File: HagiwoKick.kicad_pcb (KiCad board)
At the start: 2 copper layers, 30 x 106 mm, 37 parts, among them J1 Tune In, J2 Eurorack_Power_16pin_Shrouded, J3 A. Out, J4 Trig In

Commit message: latest updates
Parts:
- removed Attack, Decay, Harmonic, Tone: 100K, Library:Pot_9mm_DShaft_RemovedPins4_5
- removed J4: Trig In, Library:EighthInch_PJ398SM_T_TN_S
- added PWR1: Eurorack_Power_10pin_Unshrouded, Library:IDC-Header_2x05_P2.54mm_Vertical_Euro_Power_Striped_ThickerText, B.Cu at (56.9, 111.7)
- added RV1: 100k, Library:Pot_9mm_DShaft_RemovedPins4_5, F.Cu at (66.0, 57.1)
- added RV2: 100k, Library:Pot_9mm_DShaft_RemovedPins4_5, F.Cu at (66.0, 76.8)
- added RV3: 100k, Library:Pot_9mm_DShaft_RemovedPins4_5, F.Cu at (66.0, 116.1)
- added RV4: 100k, Library:Pot_9mm_DShaft_RemovedPins4_5, F.Cu at (66.0, 96.5)
- C1, C2, C3, C4, C5: value 101 -> 100pF
- C10: value 222 -> 2.2nF
- C6: value 104 -> 100nF
- C7: footprint Capacitor_THT:CP_Radial_D5.0mm_P2.50mm -> Capacitor_THT:CP_Radial_D4.0mm_P1.50mm
- C8: value 225 -> 2.2uF
- C9: value 474 -> 470nF
- D1, D2, D3, D4, D5, D6: value B43 -> BAT43; footprint Diode_THT:D_DO-35_SOD27_P7.62mm_Horizontal -> Library:D_DO-35_SOD27_P7.62mm_Horizontal_Widened_No_K
- J1: value Tune In -> TUNE CV; footprint Library:EighthInch_PJ398SM_T_TN_S -> Library:EighthInch_PJ398SM_3mmNPTH
- J2: value Eurorack_Power_16pin_Shrouded -> OUT; footprint PCM_4ms_Connector:Pins_2x08_2.54mm_TH_EuroPower_Shrouded -> Library:EighthInch_PJ398SM_3mmNPTH; moved to F.Cu
- J3: value A. Out -> TRIG; footprint Library:EighthInch_PJ398SM_T_TN_S -> Library:EighthInch_PJ398SM_3mmNPTH
- R1, R10, R2, R3, R4, R5: value 1K -> 1k
- R6, R8: value 100K -> 100k
- R7: value 33K -> 33k
- moved R1 77.3 mm to (77.5, 64.1), turned to -90 degrees
- moved C1 75.4 mm to (77.5, 74.9), turned to -90 degrees
- moved D3 69.9 mm to (67.6, 136.7), turned to -90 degrees
- moved D4 67.6 mm to (64.5, 136.7), turned to -90 degrees
- moved C8 51.6 mm to (54.6, 64.1)
- moved D1 41.1 mm to (67.6, 147.1), turned to -90 degrees
- moved D2 38.9 mm to (64.5, 147.1), turned to -90 degrees
- moved J2 35.9 mm to (58.4, 148.8), turned to -90 degrees
- moved C9 35.3 mm to (54.6, 80.6)
- moved R4 33.3 mm to (77.5, 116.1)
- moved C2 31.9 mm to (77.5, 88.8)
- moved C6 31.6 mm to (73.7, 101.4), turned to 90 degrees
- moved R2 27.7 mm to (77.5, 99.6)
- moved C7 24.4 mm to (59.4, 103.4), turned to 180 degrees
- moved D5 23.7 mm to (62.2, 109.0), turned to 0 degrees
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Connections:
- C10 pad 2: Net-(C10-Pad2) -> Net-(J2-SIG)
- J2 pad 1: Net-(J2-P1) -> Net-(J2-SIG)
- J2 pad 2: Net-(J2-P1) -> unconnected-(J2-SHEILD-Pad2)
- J2 pad 3: Net-(J2-P3) -> GND
- R10 pad 2: Net-(J4-PadT) -> Net-(J3-SIG)
- R5 pad 1: Net-(J1-PadT) -> Net-(J1-SIG)
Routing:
- net A0: track 131.5 -> 11.2 mm
- net D10: track 27.6 -> 129.1 mm, vias 3 -> 0
- net Net-(J3-SIG): track 0.00 -> 71.8 mm
- net Net-(C8-Pad1): track 80.0 -> 9.47 mm, vias 4 -> 0
- net Net-(J4-PadT): track 53.7 -> 0.00 mm
- net Net-(D7-A): track 138.5 -> 85.9 mm
- net A1: track 66.4 -> 25.8 mm
- net Net-(C10-Pad1): track 104.3 -> 66.9 mm, vias 2 -> 0
- net Net-(R3-Pad1): track 44.0 -> 10.5 mm
- net A5: track 31.6 -> 56.9 mm
- net Net-(R2-Pad1): track 46.4 -> 21.2 mm, vias 4 -> 0
- net Net-(J1-PadT): track 24.9 -> 0.00 mm
- net +5V: track 87.3 -> 110.6 mm
- net +12V: track 54.5 -> 36.2 mm
- net GND: track 13.8 -> 0.00 mm
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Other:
- board text added: "SynthLab"
- board text added: "`TR KICK` BY HAGIWO"
- board text added: "github.com/fablabnk/SynthLabProjects"
- board text removed: "`TR KICK` ORIGINAL DESIGN BY HAGIWO"

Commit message: v1.1 ready for final check
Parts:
- C7: footprint Capacitor_THT:CP_Radial_D4.0mm_P1.50mm -> Capacitor_THT:CP_Radial_D4.0mm_P2.00mm
- RV1, RV2, RV3, RV4: value 100k -> 100k B
- moved C7 0.26 mm to (59.7, 103.4)
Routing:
- net A5: track 56.9 -> 82.7 mm
- net Net-(J3-SIG): track 71.8 -> 46.8 mm
- net D10: track 129.1 -> 117.5 mm, vias 0 -> 2
- net Net-(D7-A): track 85.9 -> 96.4 mm, vias 2 -> 6
- net A6: track 101.6 -> 92.5 mm, vias 0 -> 5
- net +5V: track 110.6 -> 103.5 mm
- net Net-(R1-Pad1): track 18.7 -> 13.6 mm
- net Net-(C10-Pad1): track 66.9 -> 68.7 mm
- net A3: track 38.1 -> 39.1 mm, vias 0 -> 1
- net Net-(R2-Pad1): track 21.2 -> 21.9 mm, vias 0 -> 2
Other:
- board text added: "V1.1"
- board text removed: "V1.0"

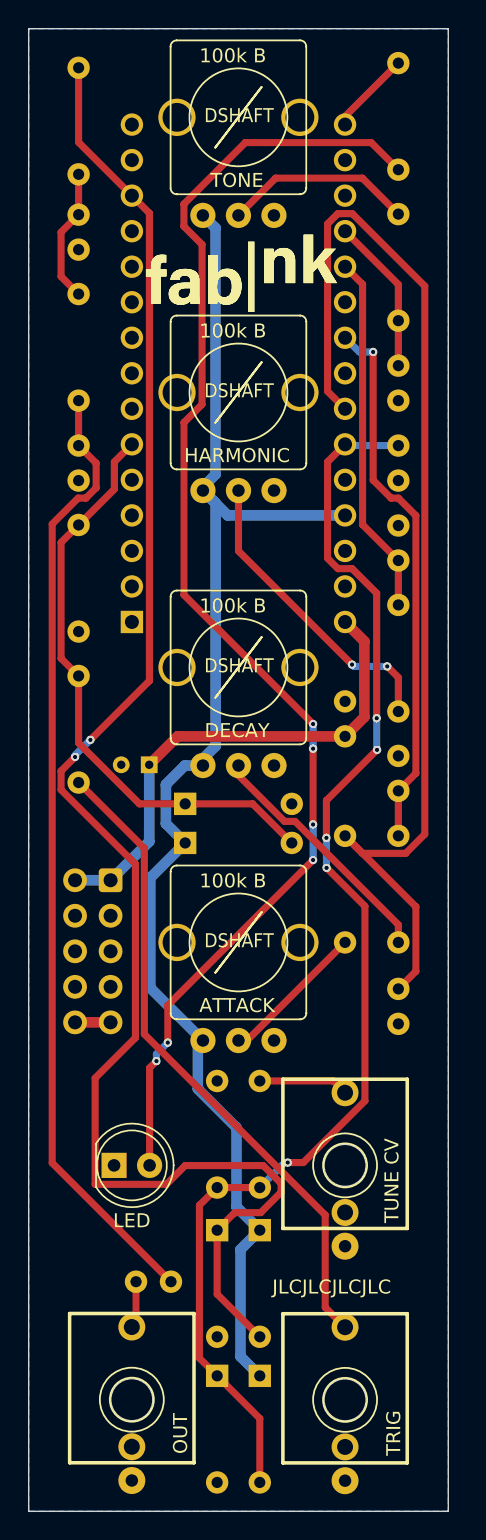
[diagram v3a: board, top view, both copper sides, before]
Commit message: switched positions of TRIG and OUT outputs
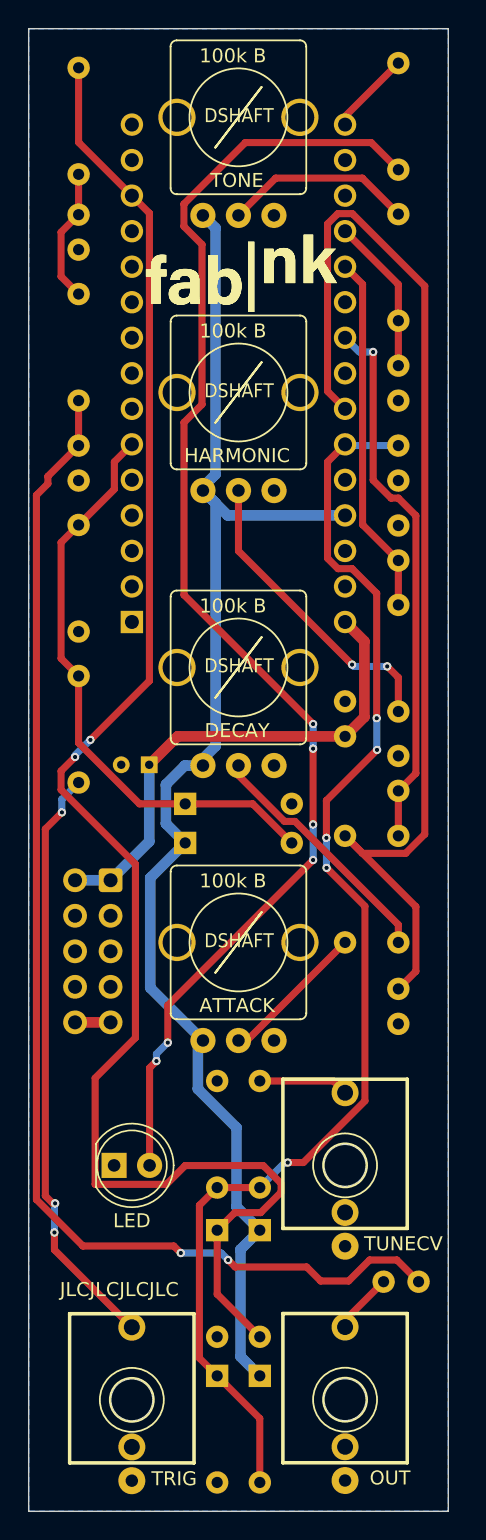
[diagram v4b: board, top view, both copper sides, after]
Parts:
- J1: value TUNE CV -> TUNECV
- moved C10 17.7 mm to (78.9, 140.4)
- moved J2 15.2 mm to (73.7, 148.8)
- moved J3 15.2 mm to (58.4, 148.8)
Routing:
- net Net-(C10-Pad1): track 68.7 -> 89.4 mm, vias 0 -> 2
- net Net-(J3-SIG): track 46.8 -> 42.6 mm, vias 0 -> 3
- net Net-(J2-SIG): track 3.36 -> 4.38 mm
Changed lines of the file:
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@@
 		(pad_to_mask_clearance 0)
 		(allow_soldermask_bridges_in_footprints no)
+		(grid_origin 58.415 148.8313)
 		(pcbplotparams
 			(layerselection 0x00010fc_ffffffff)
@@
 	(footprint "Library:EighthInch_PJ398SM_3mmNPTH"
 		(layer "F.Cu")
-		(at 58.415 148.8313 -90)
+		(at 73.66 148.8313 -90)
 		(property "Reference" "J2"
 			(at -5.0172 -4.866 90)
@@
 		)
 		(property "Value" "OUT"
-			(at 0.950657 -4.068837 -90)
+			(at 5 -1.755 0)
 			(layer "F.SilkS")
 			(effects
@@
 					(thickness 0.15)
 				)
-				(justify right bottom)
+				(justify left top)
 			)
 		)
@@
 			)
 		)
-		(property "Value" "TUNE CV"
-			(at 4.112957 -3.936837 90)
+		(property "Value" "TUNECV"
+			(at 6.1763 -1.355 180)
 			(layer "F.SilkS")
 			(effects
@@
 	(footprint "Library:EighthInch_PJ398SM_3mmNPTH"
 		(layer "F.Cu")
-		(at 73.66 148.844 -90)
+		(at 58.415 148.844 -90)
 		(property "Reference" "J3"
-			(at -5.0172 -4.866 -90)
+			(at -5.0172 -4.866 90)
 			(layer "F.SilkS")
 			(hide yes)
@@
 					(thickness 0.1524)
 				)
-				(justify left bottom)
+				(justify right top)
 			)
 		)
 		(property "Value" "TRIG"
-			(at 3.985957 -4.063837 90)
+			(at 6.2123 -1.4 180)
 			(layer "F.SilkS")
 			(effects
@@
 	(footprint "Capacitor_THT:C_Disc_D3.8mm_W2.6mm_P2.50mm"
 		(layer "B.Cu")
-		(at 61.213837 140.383957 180)
+		(at 78.915 140.383957 180)
 		(descr "C, Disc series, Radial, pin pitch=2.50mm, , diameter*width=3.8*2.6mm^2, Capacitor, http://www.vishay.com/docs/45233/krseries.pdf")
 		(tags "C Disc series Radial pin pitch 2.50mm  diameter 3.8mm width 2.6mm Capacitor")
@@
 	)
 	(gr_text "SynthLab"
-		(at 77.47 155.702 -90)
+		(at 77.47 155.702 270)
 		(layer "B.SilkS")
 		(effects
@@
 	)
 	(gr_text "JLCJLCJLCJLC"
-		(at 68.453 141.351 0)
+		(at 53.265 141.5313 0)
 		(layer "F.SilkS")
 		(effects
@@
 	)
 	(segment
-		(start 58.713837 140.383957)
-		(end 58.713837 143.325463)
+		(start 73.66 143.6243)
+		(end 73.66 143.138957)
 		(width 0.508)
 		(layer "F.Cu")
@@
 	)
 	(segment
-		(start 58.713837 143.325463)
-		(end 58.415 143.6243)
+		(start 73.66 143.138957)
+		(end 76.415 140.383957)
 		(width 0.508)
 		(layer "F.Cu")
@@
 	)
 	(segment
-		(start 52.721 86.217)
-		(end 52.721 131.89112)
+		(start 51.594 134.5103)
+		(end 54.915 137.8313)
 		(width 0.508)
 		(layer "F.Cu")
@@
 	)
 	(segment
-		(start 55.863837 83.626381)
-		(end 55.129261 84.360957)
+		(start 54.609837 80.606957)
+		(end 52.415 82.801794)
 		(width 0.508)
 		(layer "F.Cu")
@@
 	)
 	(segment
-		(start 52.721 131.89112)
-		(end 61.213837 140.383957)
+		(start 54.915 137.8313)
+		(end 61.415 137.8313)
 		(width 0.508)
 		(layer "F.Cu")
@@
 	)
 	(segment
-		(start 55.863837 81.860957)
-		(end 55.863837 83.626381)
+		(start 65.801837 139.3313)
+		(end 70.915 139.3313)
 		(width 0.508)
 		(layer "F.Cu")
@@
 	)
 	(segment
-		(start 55.129261 84.360957)
-		(end 54.577043 84.360957)
+		(start 54.61 80.606794)
+		(end 54.609837 80.606957)
 		(width 0.508)
 		(layer "F.Cu")
@@
 	)
 	(segment
-		(start 54.61 80.606794)
-		(end 54.609837 80.606957)
+		(start 52.415 83.3313)
+		(end 51.594 84.1523)
 		(width 0.508)
 		(layer "F.Cu")
@@
 	)
 	(segment
-		(start 54.577043 84.360957)
-		(end 52.721 86.217)
+		(start 52.415 82.801794)
+		(end 52.415 83.3313)
 		(width 0.508)
 		(layer "F.Cu")
@@
 	)
 	(segment
-		(start 54.609837 80.606957)
-		(end 55.863837 81.860957)
+		(start 61.415 137.8313)
+		(end 61.915 138.3313)
+		(width 0.508)
+		(layer "F.Cu")
+		(net 32)
+	)
+	(segment
+		(start 73.915 140.3313)
+		(end 75.415 138.8313)
+		(width 0.508)
+		(layer "F.Cu")
+		(net 32)
+	)
+	(segment
+		(start 70.915 139.3313)
+		(end 71.915 140.3313)
+		(width 0.508)
+		(layer "F.Cu")
+		(net 32)
+	)
+	(segment
+		(start 65.301837 138.8313)
+		(end 65.801837 139.3313)
+		(width 0.508)
+		(layer "F.Cu")
+		(net 32)
+	)
+	(segment
+		(start 51.594 84.1523)
+		(end 51.594 134.5103)
+		(width 0.508)
+		(layer "F.Cu")
+		(net 32)
+	)
+	(segment
+		(start 71.915 140.3313)
+		(end 73.915 140.3313)
+		(width 0.508)
+		(layer "F.Cu")
+		(net 32)
+	)
+	(segment
+		(start 75.415 138.8313)
+		(end 77.362343 138.8313)
+		(width 0.508)
+		(layer "F.Cu")
+		(net 32)
+	)
+	(segment
+		(start 77.362343 138.8313)
+		(end 78.915 140.383957)
 		(width 0.508)
 		(layer "F.Cu")
 		(net 32)
 	)
+	(via
+		(at 61.915 138.3313)
+		(size 0.6)
+		(drill 0.3)
+		(layers "F.Cu" "B.Cu")
+		(net 32)
+	)
+	(via
+		(at 65.301837 138.8313)
+		(size 0.6)
+		(drill 0.3)
+		(layers "F.Cu" "B.Cu")
+		(net 32)
+	)
+	(segment
+		(start 64.801837 138.3313)
+		(end 65.301837 138.8313)
+		(width 0.508)
+		(layer "B.Cu")
+		(net 32)
+	)
+	(segment
+		(start 61.915 138.3313)
+		(end 64.801837 138.3313)
+		(width 0.508)
+		(layer "B.Cu")
+		(net 32)
+	)
 	(segment
 		(start 60.985159 120.624841)
@@
 	)
 	(segment
-		(start 72.2408 142.2178)
-		(end 72.2408 135.6138)
+		(start 52.763287 134.781561)
+		(end 52.229 134.247274)
 		(width 0.508)
 		(layer "F.Cu")
@@
 	)
 	(segment
-		(start 59.309 109.395957)
-		(end 54.61 104.696957)
+		(start 58.415 143.637)
+		(end 52.881841 138.103841)
+		(width 0.508)
+		(layer "F.Cu")
+		(net 37)
+	)
+	(segment
+		(start 52.229 108.0173)
+		(end 53.415 106.8313)
 		(width 0.508)
 		(layer "F.Cu")
@@
 	)
 	(segment
-		(start 59.309 122.682)
-		(end 59.309 109.395957)
+		(start 52.93158 134.781561)
+		(end 52.763287 134.781561)
 		(width 0.508)
 		(layer "F.Cu")
@@
 	)
 	(segment
-		(start 73.66 143.637)
-		(end 72.2408 142.2178)
+		(start 52.229 134.247274)
+		(end 52.229 108.0173)
 		(width 0.508)
 		(layer "F.Cu")
@@
 	)
 	(segment
-		(start 72.2408 135.6138)
-		(end 59.309 122.682)
+		(start 52.881841 138.103841)
+		(end 52.881841 136.864459)
 		(width 0.508)
 		(layer "F.Cu")
 		(net 37)
 	)
+	(via
+		(at 53.415 106.8313)
+		(size 0.6)
+		(drill 0.3)
+		(layers "F.Cu" "B.Cu")
+		(net 37)
+	)
+	(via
+		(at 52.881841 136.864459)
+		(size 0.6)
+		(drill 0.3)
+		(layers "F.Cu" "B.Cu")
+		(net 37)
+	)
+	(via
+		(at 52.93158 134.781561)
+		(size 0.6)
+		(drill 0.3)
+		(layers "F.Cu" "B.Cu")
+		(net 37)
+	)
+	(segment
+		(start 53.415 106.8313)
+		(end 53.415 105.891957)
+		(width 0.508)
+		(layer "B.Cu")
+		(net 37)
+	)
+	(segment
+		(start 52.93158 134.781561)
+		(end 52.881841 134.8313)
+		(width 0.508)
+		(layer "B.Cu")
+		(net 37)
+	)
+	(segment
+		(start 52.881841 134.8313)
+		(end 52.881841 136.864459)
+		(width 0.508)
+		(layer "B.Cu")
+		(net 37)
+	)
+	(segment
+		(start 53.415 105.891957)
+		(end 54.61 104.696957)
+		(width 0.508)
+		(layer "B.Cu")
+		(net 37)
+	)

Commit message: reversed orientated of pots on schematic to make +5V rightmost pin and updated routing. This completes v1.2
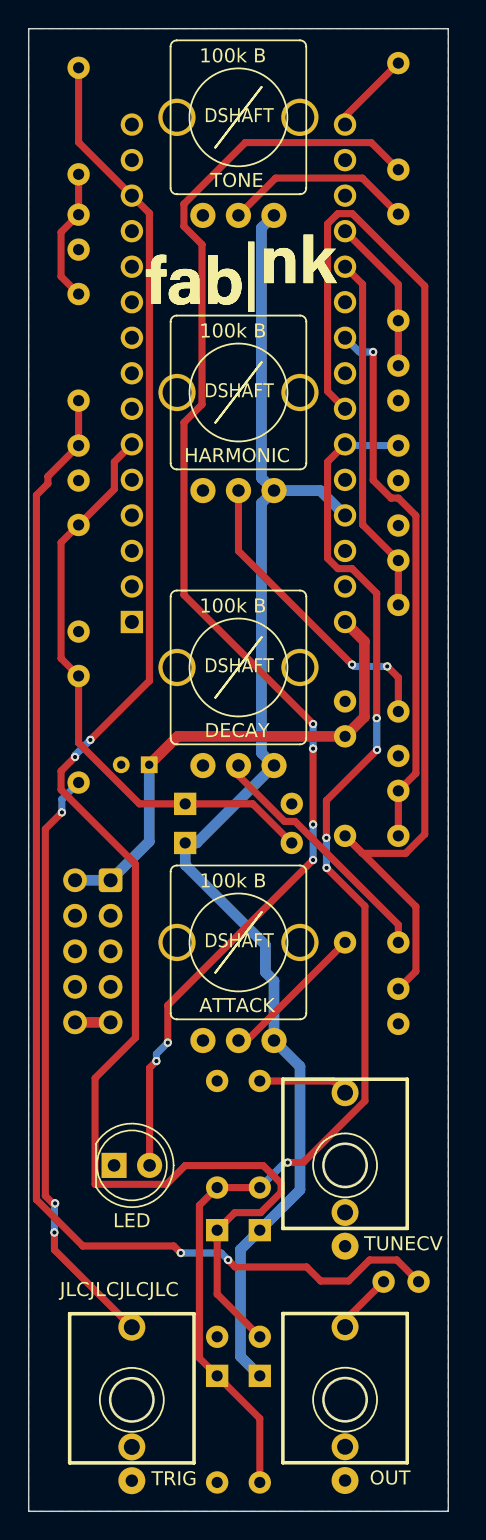
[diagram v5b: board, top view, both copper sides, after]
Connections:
- RV1 pad 1: +5V -> GND
- RV1 pad 3: GND -> +5V
- RV2 pad 1: +5V -> GND
- RV2 pad 3: GND -> +5V
- RV3 pad 1: +5V -> GND
- RV3 pad 3: GND -> +5V
- RV4 pad 1: +5V -> GND
- RV4 pad 3: GND -> +5V
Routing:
- net +5V: track 103.5 -> 99.1 mm
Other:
- board text added: "V1.2"
- board text removed: "V1.1"
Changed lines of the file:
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@@
 			(layers "*.Cu" "*.Mask")
 			(remove_unused_layers no)
-			(net 16 "+5V")
+			(net 12 "GND")
 			(pinfunction "1")
 			(pintype "passive")
@@
 			(layers "*.Cu" "*.Mask")
 			(remove_unused_layers no)
-			(net 12 "GND")
+			(net 16 "+5V")
 			(pinfunction "3")
 			(pintype "passive")
@@
 			(layers "*.Cu" "*.Mask")
 			(remove_unused_layers no)
-			(net 16 "+5V")
+			(net 12 "GND")
 			(pinfunction "1")
 			(pintype "passive")
@@
 			(layers "*.Cu" "*.Mask")
 			(remove_unused_layers no)
-			(net 12 "GND")
+			(net 16 "+5V")
 			(pinfunction "3")
 			(pintype "passive")
@@
 			(layers "*.Cu" "*.Mask")
 			(remove_unused_layers no)
-			(net 16 "+5V")
+			(net 12 "GND")
 			(pinfunction "1")
 			(pintype "passive")
@@
 			(layers "*.Cu" "*.Mask")
 			(remove_unused_layers no)
-			(net 12 "GND")
+			(net 16 "+5V")
 			(pinfunction "3")
 			(pintype "passive")
@@
 			(layers "*.Cu" "*.Mask")
 			(remove_unused_layers no)
-			(net 16 "+5V")
+			(net 12 "GND")
 			(pinfunction "1")
 			(pintype "passive")
@@
 			(layers "*.Cu" "*.Mask")
 			(remove_unused_layers no)
-			(net 12 "GND")
+			(net 16 "+5V")
 			(pinfunction "3")
 			(pintype "passive")
@@
 		)
 	)
-	(gr_text "V1.1"
+	(gr_text "V1.2"
 		(at 52.07 155.702 270)
 		(layer "B.SilkS" knockout)
@@
 	)
 	(segment
-		(start 63.500163 83.821843)
-		(end 63.500163 83.565837)
-		(width 0.762)
-		(layer "B.Cu")
-		(net 16)
-	)
-	(segment
-		(start 63.500163 103.481443)
-		(end 63.500163 102.996837)
-		(width 0.762)
-		(layer "B.Cu")
-		(net 16)
-	)
-	(segment
-		(start 60.848837 104.839957)
-		(end 62.207351 103.481443)
-		(width 0.762)
-		(layer "B.Cu")
-		(net 16)
-	)
-	(segment
-		(start 59.7313 119.3705)
-		(end 59.7313 111.513494)
+		(start 70.438659 133.826135)
+		(end 67.563837 136.700957)
 		(width 0.762)
 		(layer "B.Cu")
@@
 	)
 	(segment
-		(start 63.134837 126.604986)
-		(end 63.134837 123.504363)
+		(start 68.58 118.8713)
+		(end 68.58 123.1392)
 		(width 0.762)
 		(layer "B.Cu")
@@
 	)
 	(segment
-		(start 64.396863 65.051243)
-		(end 63.495163 64.149543)
+		(start 68.580163 103.481443)
+		(end 67.678463 102.579743)
 		(width 0.762)
 		(layer "B.Cu")
@@
 	)
 	(segment
-		(start 65.27632 85.598)
-		(end 63.500163 83.821843)
+		(start 67.678463 102.579743)
+		(end 67.678463 84.723543)
 		(width 0.762)
 		(layer "B.Cu")
@@
 	)
 	(segment
-		(start 63.134837 123.504363)
-		(end 63.5 123.1392)
+		(start 63.046649 109.014957)
+		(end 68.580163 103.481443)
 		(width 0.762)
 		(layer "B.Cu")
@@
 	)
 	(segment
-		(start 67.563837 136.700957)
-		(end 65.896837 135.033957)
+		(start 67.678463 84.723543)
+		(end 68.580163 83.821843)
 		(width 0.762)
 		(layer "B.Cu")
@@
 	)
 	(segment
-		(start 64.401863 84.723543)
-		(end 63.500163 83.821843)
+		(start 67.678463 65.046243)
+		(end 68.575163 64.149543)
 		(width 0.762)
 		(layer "B.Cu")
@@
 	)
 	(segment
-		(start 65.896837 135.033957)
-		(end 65.896837 129.366986)
+		(start 62.229837 109.014957)
+		(end 63.046649 109.014957)
 		(width 0.762)
 		(layer "B.Cu")
@@
 	)
 	(segment
-		(start 66.182837 145.733957)
-		(end 66.182837 138.081957)
+		(start 68.58 123.1392)
+		(end 70.438659 124.997859)
 		(width 0.762)
 		(layer "B.Cu")
@@
 	)
 	(segment
-		(start 65.896837 129.366986)
-		(end 63.134837 126.604986)
+		(start 70.438659 124.997859)
+		(end 70.438659 133.826135)
 		(width 0.762)
 		(layer "B.Cu")
@@
 	)
 	(segment
-		(start 63.500163 83.565837)
-		(end 64.396863 82.669137)
+		(start 71.883843 83.821843)
+		(end 73.66 85.598)
 		(width 0.762)
 		(layer "B.Cu")
@@
 	)
 	(segment
-		(start 64.396863 82.669137)
-		(end 64.396863 65.051243)
+		(start 67.965 118.2563)
+		(end 68.58 118.8713)
 		(width 0.762)
 		(layer "B.Cu")
@@
 	)
 	(segment
-		(start 59.7313 111.513494)
-		(end 62.229837 109.014957)
+		(start 66.182837 145.733957)
+		(end 66.182837 138.081957)
 		(width 0.762)
 		(layer "B.Cu")
@@
 	)
 	(segment
-		(start 63.500163 102.996837)
-		(end 64.401863 102.095137)
+		(start 68.580163 83.821843)
+		(end 67.678463 82.920143)
 		(width 0.762)
 		(layer "B.Cu")
@@
 	)
 	(segment
-		(start 73.66 85.598)
-		(end 65.27632 85.598)
+		(start 68.580163 83.821843)
+		(end 71.883843 83.821843)
 		(width 0.762)
 		(layer "B.Cu")
@@
 	)
 	(segment
-		(start 64.401863 102.095137)
-		(end 64.401863 84.723543)
+		(start 67.678463 82.920143)
+		(end 67.678463 65.046243)
 		(width 0.762)
 		(layer "B.Cu")
@@
 	)
 	(segment
-		(start 60.848837 107.633957)
-		(end 60.848837 104.839957)
+		(start 62.229837 109.014957)
+		(end 62.229837 110.576957)
 		(width 0.762)
 		(layer "B.Cu")
@@
 	)
 	(segment
-		(start 62.229837 109.014957)
-		(end 60.848837 107.633957)
+		(start 67.965 116.31212)
+		(end 67.965 118.2563)
 		(width 0.762)
 		(layer "B.Cu")
@@
 	)
 	(segment
-		(start 63.5 123.1392)
-		(end 59.7313 119.3705)
-		(width 0.762)
-		(layer "B.Cu")
-		(net 16)
-	)
-	(segment
-		(start 62.207351 103.481443)
-		(end 63.500163 103.481443)
+		(start 62.229837 110.576957)
+		(end 67.965 116.31212)
 		(width 0.762)
 		(layer "B.Cu")
